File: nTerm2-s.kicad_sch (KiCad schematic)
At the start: 105 parts, among them J1 VGA, J2 Keyboard, J3 Mouse, J4 Speaker, J5 DE9_Plug_MountingHoles, J6 USB_B_Micro, K1 IM41 3V, K2 IM41 3V, K3 IM41 3V, Q1 BC817, Q2 BC817, Q3 BC817, Q4 BC817, Q5 BC817, SW1 IO0, SW2 RESET, SW3 DEFAULTS, U1 ESP32-WROOM-32, U2 LM386, U3 MAX3232E, U4 CP2102N-Axx-xQFN28, U5 NCP1117-3.3_SOT223

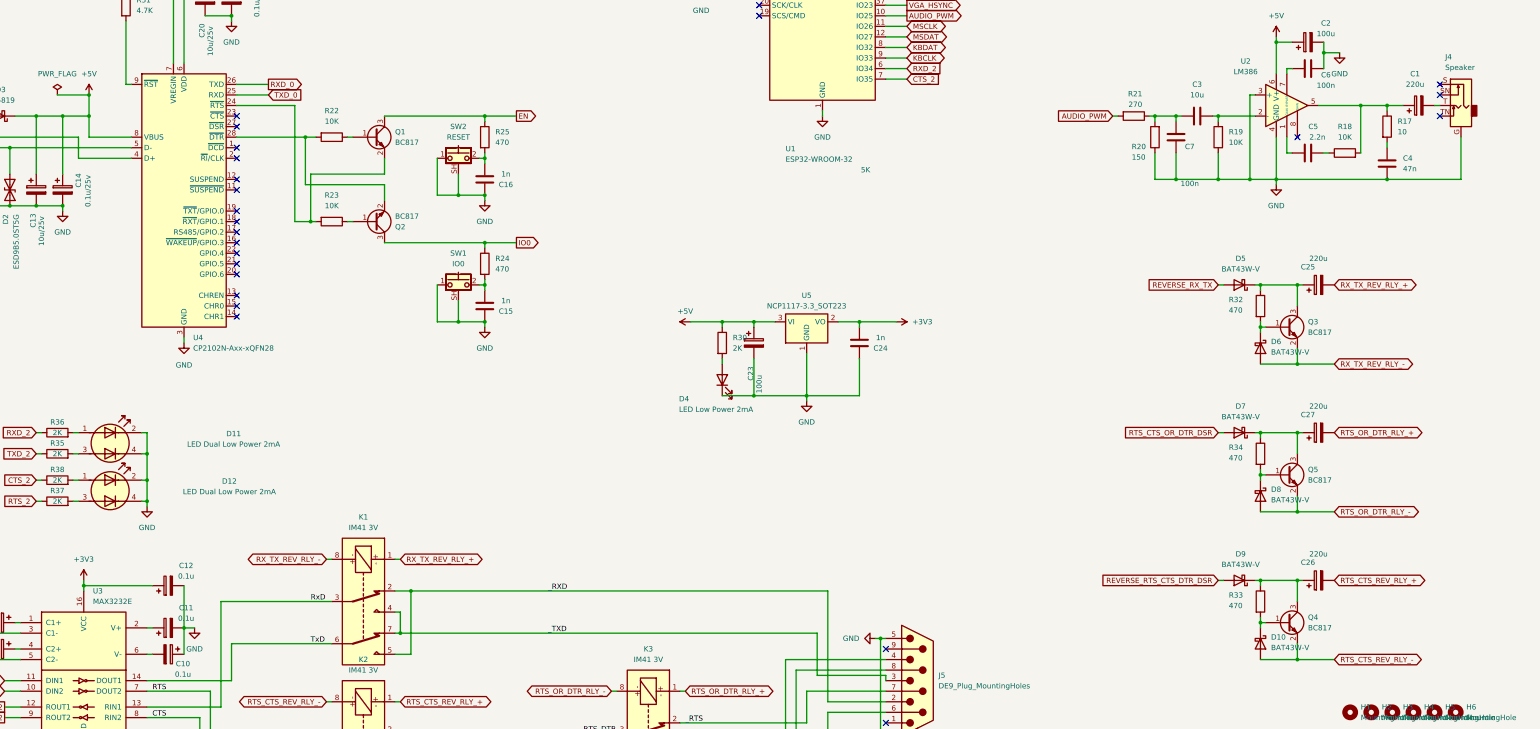
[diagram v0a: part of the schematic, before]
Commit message: Improvements: - Move 'defaults' button to side, to create space for extra mounting holes. - Change type of USB pug to one with through-hole mounts for extra strength. - Fix audio plug. - Keep some distance around Audio PWM route so we won't get crossover. - Fix missing GND connections on the relay drivers. - Many small improvements to routes. - Relay drivers are tested on breadboard and should work. - Design complete? Maybe an improvement: add SD card slot?
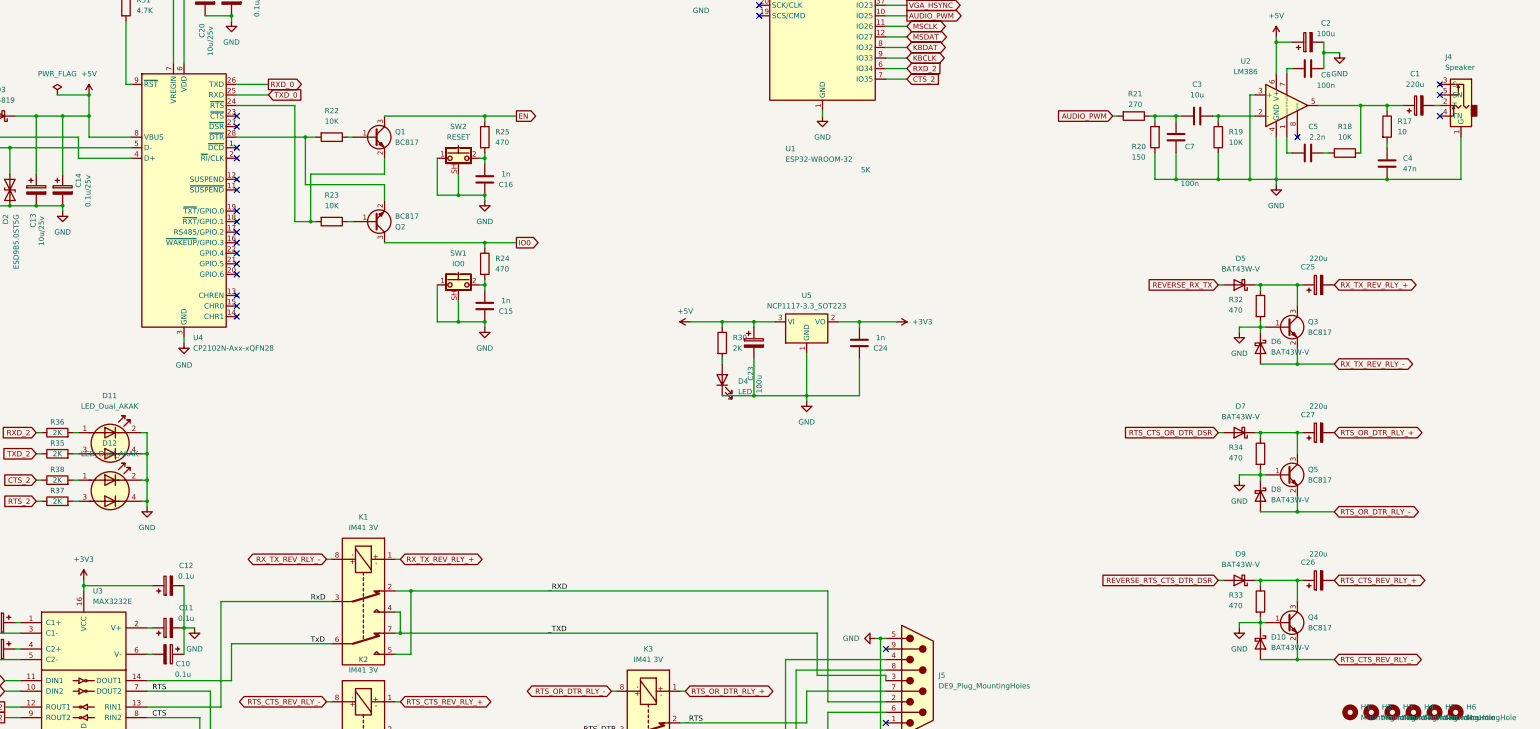
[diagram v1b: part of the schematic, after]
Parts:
- removed D4: LED Low Power 2mA, LED_THT:DIALIGHT_LED_3MM_SINGLE, symbol Device:LED
- added D4: LED, LED_THT:DIALIGHT_LED_3MM_SINGLE, symbol Device:LED pins reversed
- D11, D12: value LED Dual Low Power 2mA -> LED_Dual_AKAK
- J6: footprint SDBox-mini:USB_Micro-B_Unknown_5s_SMT -> Connector_USB:USB_Micro-B_Amphenol_10118194-0001LF_Horizontal
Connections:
- net GND: now also D10.1 (K), D6.1 (K), D8.1 (K), J4.1 (G), Q3.1 (B), Q4.1 (B), Q5.1 (B), R32.2, R33.2, R34.2, D4.2 (K); no longer J4.G
- net at R30.2: now also D4.1 (A)
- net at C1.2: now also J4.2 (T); no longer J4.T

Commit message: Made board smaller for easier fitting in enclosure (150x55 or so). Many fixes. All vias are on 1.27 grid. USB-C ocnnector. VGA signal lines all same length, hopefully helping to give good video output.
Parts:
- removed C17: 1n, Capacitor_SMD:C_0603_1608Metric_Pad1.08x0.95mm_HandSolder, symbol Device:C
- removed J6: USB_B_Micro, Connector_USB:USB_Micro-B_Amphenol_10118194-0001LF_Horizontal, symbol Connector:USB_B_Micro
- added C17: 1u, Capacitor_Tantalum_SMD:CP_EIA-3216-18_Kemet-A_Pad1.58x1.35mm_HandSolder, symbol Device:C_Polarized
- added J6: USB_C_Receptacle_USB2.0_16P, Connector_USB:USB_C_Receptacle_Molex_213716-0001, symbol Connector:USB_C_Receptacle_USB2.0_16P
- C19: value 1u -> 0.1u
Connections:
- net EN: now also C17.1
- net GND: now also J4.G (1), C17.2, J6.A1 (GND), J6.A12 (GND), J6.B1 (GND), J6.B12 (GND), J6.S1 (SHIELD); no longer J4.1 (G)
- net at D3.2 (A): now also J6.A4 (VBUS), J6.A9 (VBUS), J6.B4 (VBUS), J6.B9 (VBUS)
- net at D1.2 (A2), U4.4 (D+): now also J6.A6 (D+), J6.B6 (D+)
- net at C1.2: now also J4.T (2); no longer J4.2 (T)
- net at D2.2 (A2), U4.5 (D-): now also J6.A7 (D-), J6.B7 (D-)
- no-connect marks 40 -> 43
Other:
- company: Sporos Techno -> Sporos Tech
- moved on the sheet: C13, C14, C15, C16, C18, C19, C20, C21, D1, D2, D3, Q1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

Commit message: * Final details sorted. Hopefully I've got it all now. * Generated gerbers and sent to JLCPCB for boards to be made. * Fuses for my Fluke 175 multimeter arrived. Experimented with the relay driving circuit. When using 3.3V, 1N4148, BC337, 470u and 3K9, the circuit seems to switch quite reliably. Real circuit is meant to use BAT43 and BC817, but is probably similar enough. Can't switch too fast or the circuit will latch up and stop switching, but 4 times per second seems fine. Circuit uses some 10mA max when switching, and about 1mA continuous when the input is 3.3V.
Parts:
- C25, C26, C27: value 220u -> 470u
- R32, R33, R34: value 470 -> 3K9
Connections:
- net GND: now also J2.7, J3.7
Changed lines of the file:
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@@
 	)
 	(junction
+		(at 105.41 48.26)
+		(diameter 0)
+		(color 0 0 0 0)
+	)
+	(junction
 		(at 367.03 101.6)
 		(diameter 0)
@@
 	)
 	(junction
+		(at 48.26 48.26)
+		(diameter 0)
+		(color 0 0 0 0)
+	)
+	(junction
 		(at 135.89 262.89)
 		(diameter 0)
@@
 	(wire
 		(pts
-			(xy 105.41 40.64) (xy 105.41 46.99)
+			(xy 105.41 40.64) (xy 105.41 48.26)
 		)
 		(stroke
@@
 	(wire
 		(pts
-			(xy 48.26 40.64) (xy 48.26 46.99)
+			(xy 48.26 40.64) (xy 48.26 48.26)
 		)
 		(stroke
@@
 	(wire
 		(pts
+			(xy 96.52 48.26) (xy 105.41 48.26)
+		)
+		(stroke
+			(width 0)
+			(type default)
+		)
+	)
+	(wire
+		(pts
 			(xy 342.9 154.94) (xy 344.17 154.94)
 		)
@@
 	(wire
 		(pts
+			(xy 39.37 48.26) (xy 48.26 48.26)
+		)
+		(stroke
+			(width 0)
+			(type default)
+		)
+	)
+	(wire
+		(pts
 			(xy 50.8 36.83) (xy 50.8 43.18)
 		)
@@
 			)
 		)
-		(property "Value" "220u"
+		(property "Value" "470u"
 			(at 356.87 138.43 90)
 			(effects
@@
 			)
 		)
-		(property "Value" "220u"
+		(property "Value" "470u"
 			(at 356.87 173.99 90)
 			(effects
@@
 		(pin "T"
 		)
-		(pin "S"
+		(pin "R"
 		)
-		(pin "SN"
+		(pin "RN"
 		)
 		(instances
@@
 	(symbol
 		(lib_id "power:GND")
-		(at 48.26 46.99 0)
+		(at 48.26 48.26 0)
 		(unit 1)
 		(exclude_from_sim no)
@@
 		(fields_autoplaced yes)
 		(property "Reference" "#PWR03"
-			(at 48.26 53.34 0)
+			(at 48.26 54.61 0)
 			(effects
 				(font
@@
 		)
 		(property "Value" "GND"
-			(at 48.26 52.07 0)
+			(at 48.26 53.34 0)
 			(effects
 				(font
@@
 		)
 		(property "Footprint" ""
-			(at 48.26 46.99 0)
+			(at 48.26 48.26 0)
 			(effects
 				(font
@@
 		)
 		(property "Datasheet" ""
-			(at 48.26 46.99 0)
+			(at 48.26 48.26 0)
 			(effects
 				(font
@@
 		)
 		(property "Description" "Power symbol creates a global label with name \"GND\" , ground"
-			(at 48.26 46.99 0)
+			(at 48.26 48.26 0)
 			(effects
 				(font
@@
 		(pin "3"
 		)
+		(pin "7"
+		)
 		(instances
 			(project "nTerm2-s"
@@
 			)
 		)
-		(property "Value" "220u"
+		(property "Value" "470u"
 			(at 356.87 209.55 90)
 			(effects
@@
 			)
 		)
-		(property "Value" "470"
+		(property "Value" "3K9"
 			(at 335.28 221.996 0)
 			(effects
@@
 	(symbol
 		(lib_id "power:GND")
-		(at 105.41 46.99 0)
+		(at 105.41 48.26 0)
 		(unit 1)
 		(exclude_from_sim no)
@@
 		(fields_autoplaced yes)
 		(property "Reference" "#PWR06"
-			(at 105.41 53.34 0)
+			(at 105.41 54.61 0)
 			(effects
 				(font
@@
 		)
 		(property "Value" "GND"
-			(at 105.41 52.07 0)
+			(at 105.41 53.34 0)
 			(effects
 				(font
@@
 		)
 		(property "Footprint" ""
-			(at 105.41 46.99 0)
+			(at 105.41 48.26 0)
 			(effects
 				(font
@@
 		)
 		(property "Datasheet" ""
-			(at 105.41 46.99 0)
+			(at 105.41 48.26 0)
 			(effects
 				(font
@@
 		)
 		(property "Description" "Power symbol creates a global label with name \"GND\" , ground"
-			(at 105.41 46.99 0)
+			(at 105.41 48.26 0)
 			(effects
 				(font
@@
 	)
 	(symbol
+		(lib_name "Mini-DIN-6_1")
 		(lib_id "Connector:Mini-DIN-6")
 		(at 39.37 40.64 0)
@@
 		(pin "3"
 		)
+		(pin "7"
+		)
 		(instances
 			(project ""
@@
 			)
 		)
-		(property "Value" "470"
+		(property "Value" "3K9"
 			(at 335.28 186.436 0)
 			(effects
@@
 			)
 		)
-		(property "Value" "470"
+		(property "Value" "3K9"
 			(at 335.28 150.876 0)
 			(effects

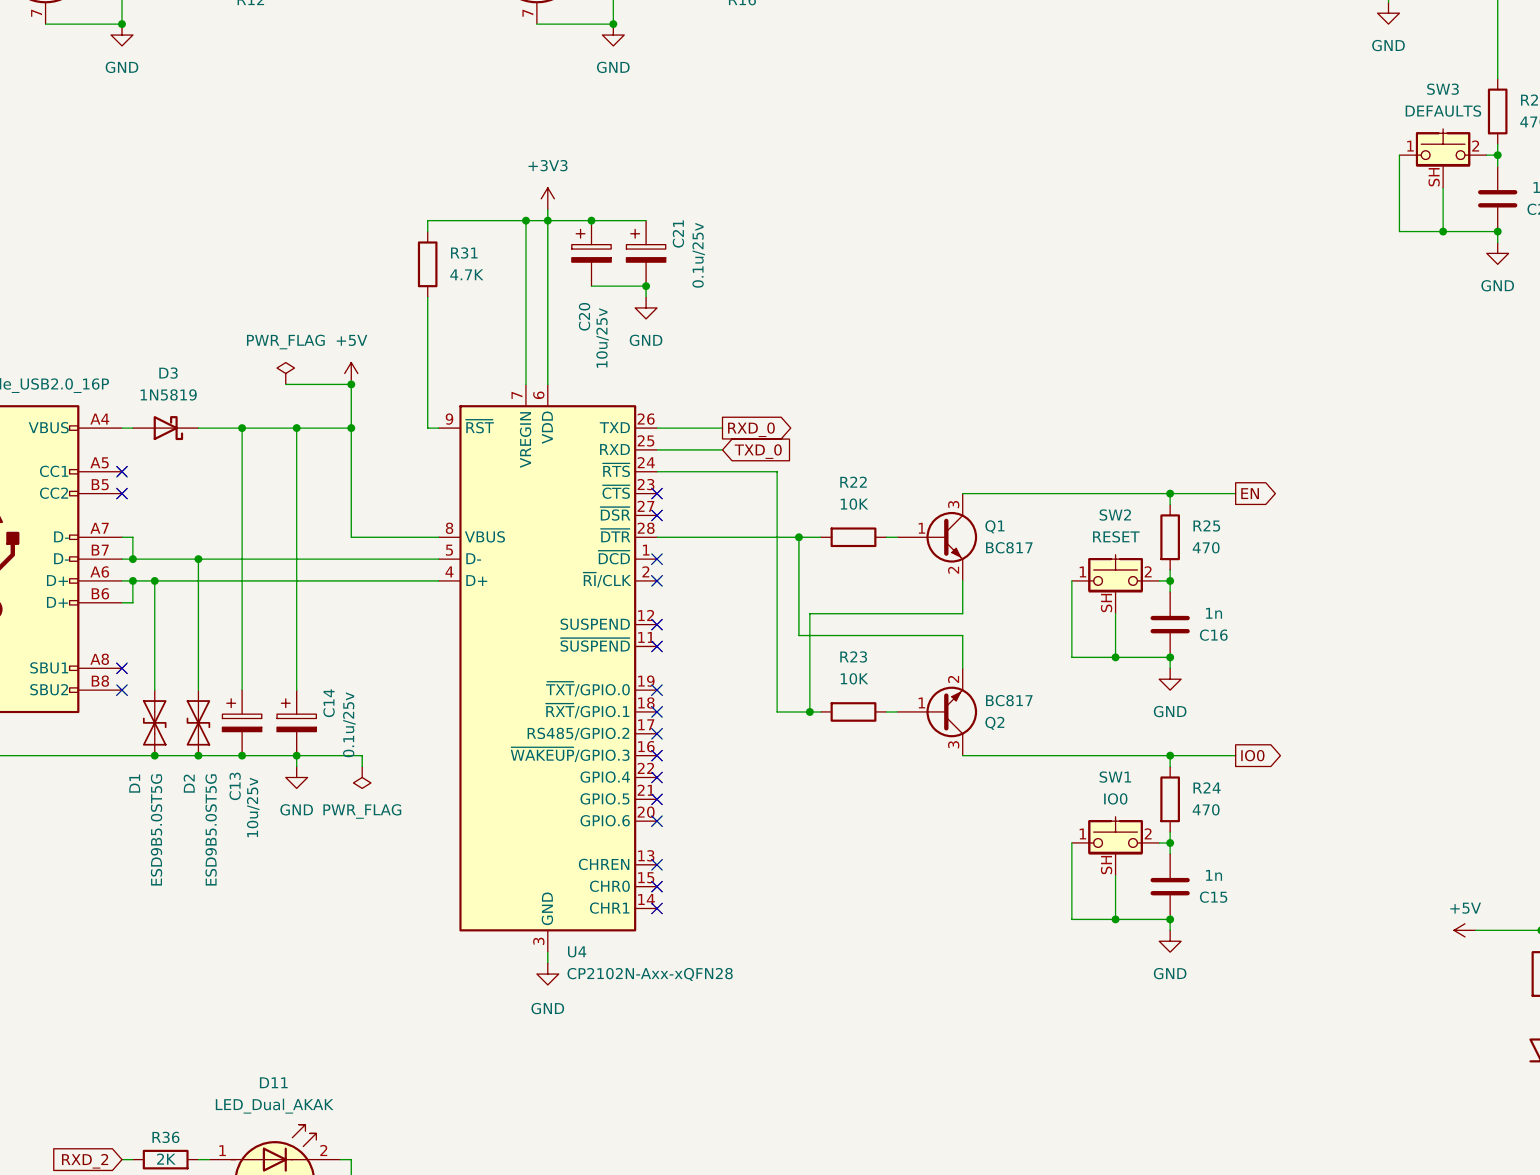
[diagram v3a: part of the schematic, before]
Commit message: Update wrong footprint for relays K1..K3.
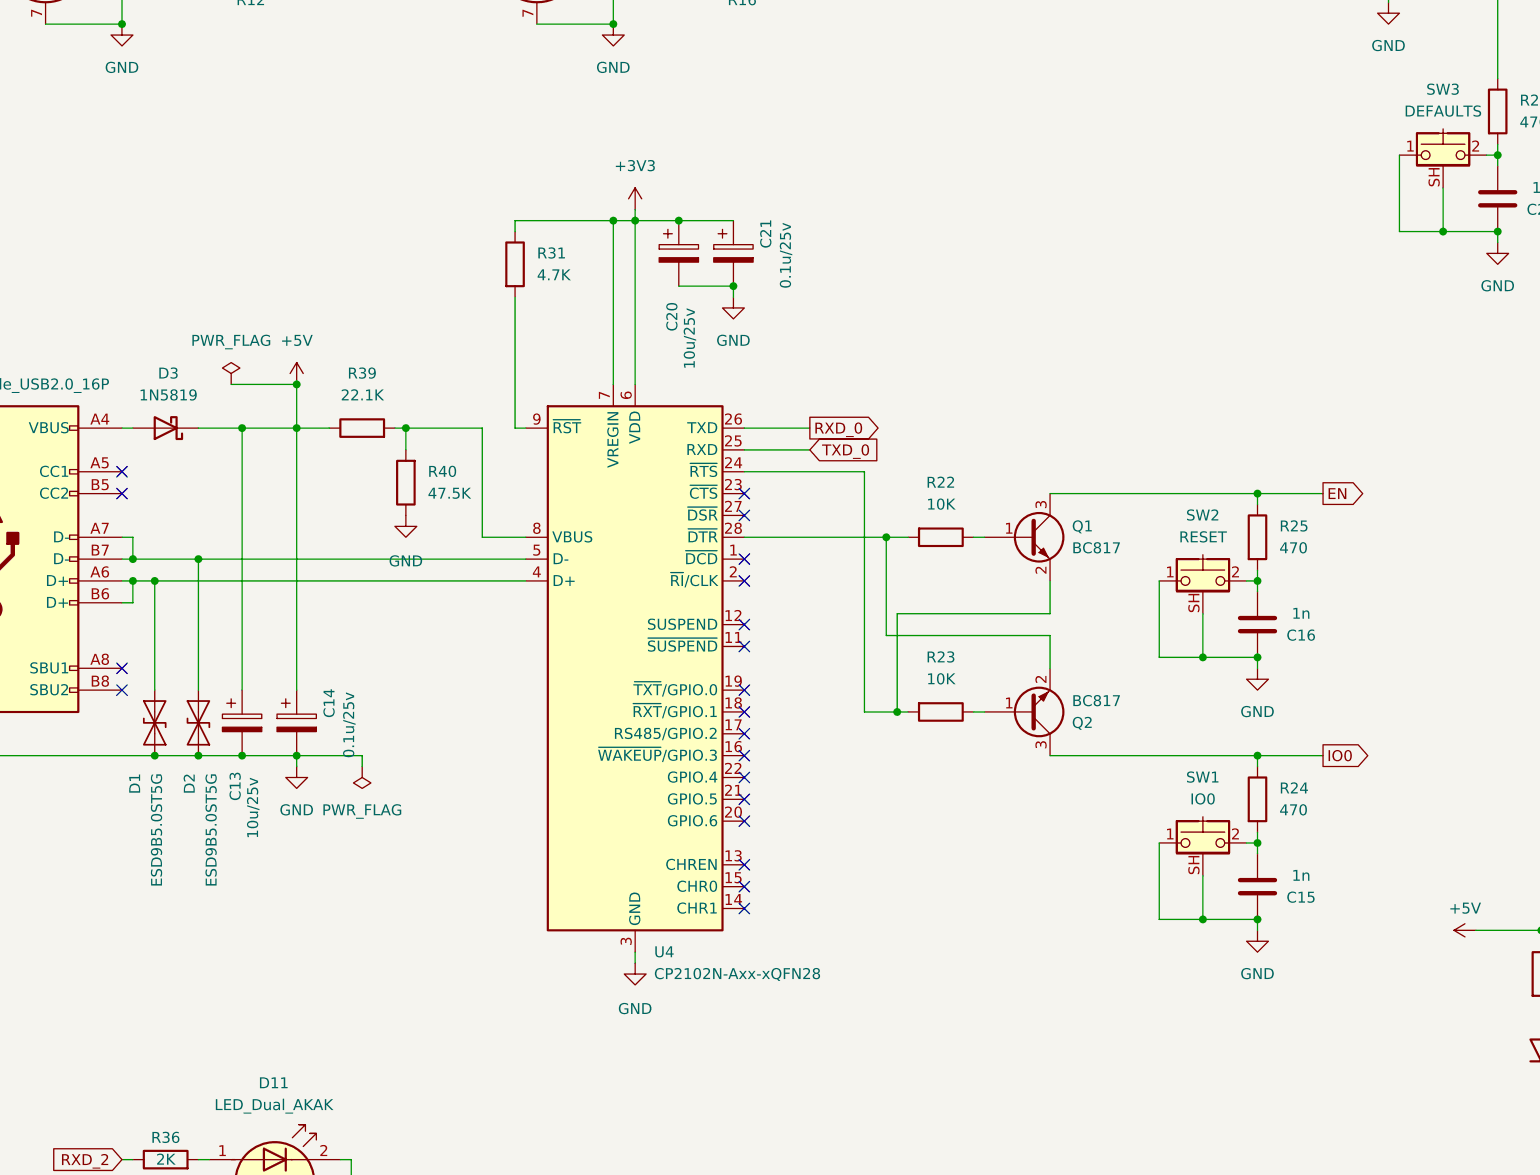
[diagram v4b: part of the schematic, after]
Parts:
- added R39: 22.1K, Resistor_SMD:R_0603_1608Metric_Pad0.98x0.95mm_HandSolder, symbol Device:R
- added R40: 47.5K, Resistor_SMD:R_0603_1608Metric_Pad0.98x0.95mm_HandSolder, symbol Device:R
- K1, K2, K3: footprint Relay_SMD:Relay_DPDT_AXICOM_IMSeries_JLeg -> Relay_SMD:Relay_2P2T_10x6mm_TE_IMxxG
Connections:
- net +5V: now also R39.1; no longer U4.8 (VBUS)
- net GND: now also R40.1
- new net: R39.2, R40.2, U4.8 (VBUS)
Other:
- moved on the sheet: C15, C16, C20, C21, Q1, Q2, R22, R23, R24, R25, R31, SW1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
